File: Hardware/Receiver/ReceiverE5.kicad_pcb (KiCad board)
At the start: 2 copper layers, 50 x 30 mm, 43 parts, among them J1 KBUS, J2 AVR-PDI-6A, J3 CONN_01X08, J4 CONN_01X06, J5 CONN_01X06, J6 CONN_01X04, J7 CONN_01X04, U1 ATXMEGA32E5-A, U2 LM2731, U3 SN74LV07A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

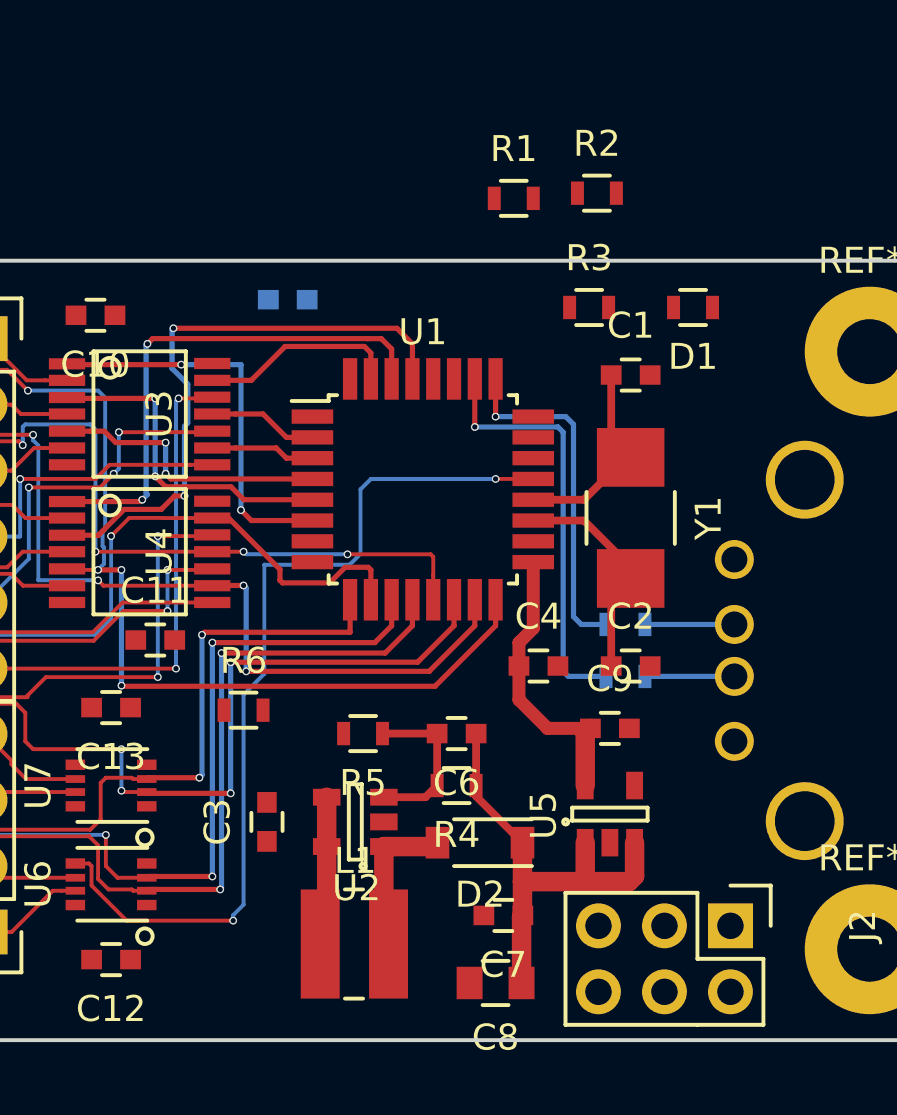
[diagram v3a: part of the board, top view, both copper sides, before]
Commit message: Finished signal routing
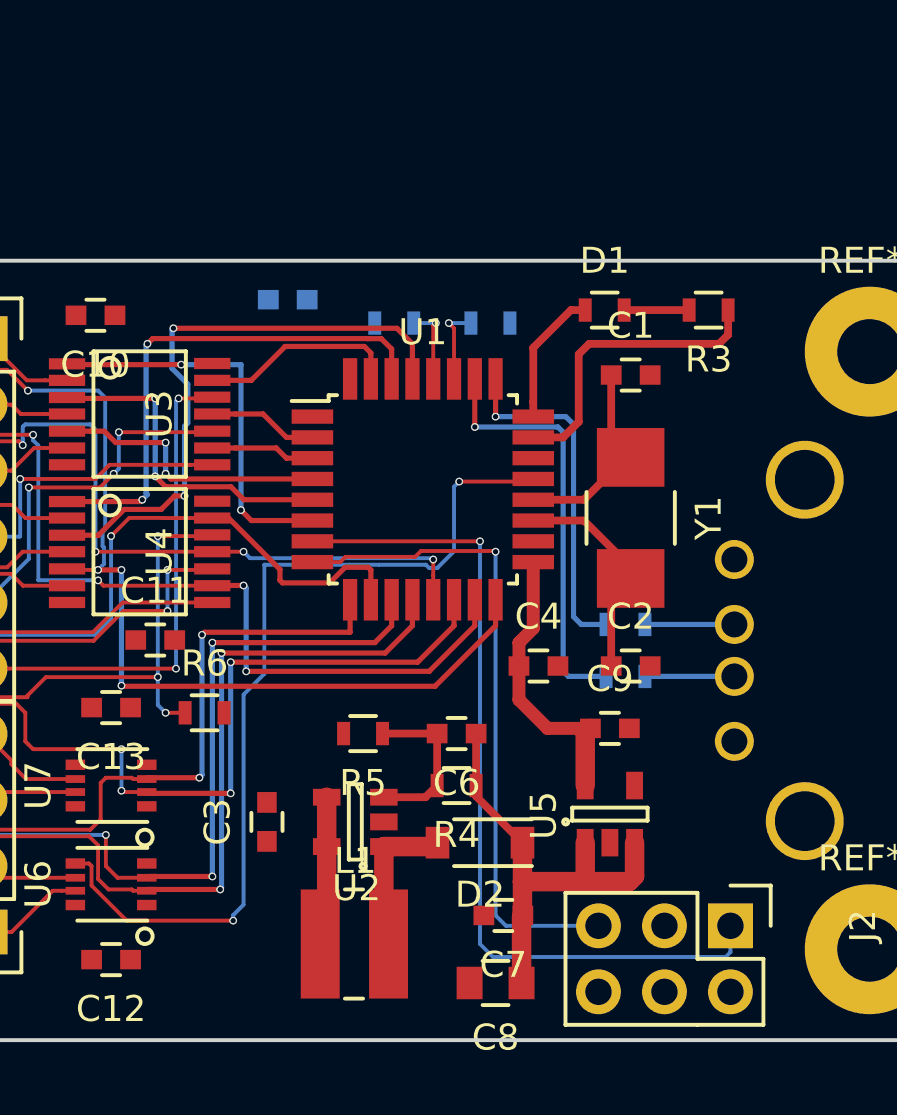
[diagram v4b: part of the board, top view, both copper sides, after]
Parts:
- R1, R2: moved to B.Cu
- moved R1 6.65 mm to (95.2, 65.4), turned to 180 degrees
- moved R2 6.47 mm to (98.9, 65.4)
- moved R3 4.60 mm to (107.3, 64.9), turned to 180 degrees
- moved D1 3.40 mm to (103.3, 64.9), turned to 0 degrees
- moved R6 1.50 mm to (87.9, 80.4)
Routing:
- net Net-(J2-Pad1): track 0.00 -> 32.9 mm, vias 0 -> 1
- net Net-(J2-Pad5): track 0.00 -> 25.4 mm, vias 0 -> 1
- net Net-(R3-Pad1): track 0.00 -> 11.6 mm
- net Net-(D1-Pad1): track 0.00 -> 5.25 mm
- net /OPT2: track 0.00 -> 3.08 mm, vias 0 -> 1
- net /OPT1: track 0.00 -> 3.04 mm, vias 0 -> 1
- net Net-(D1-Pad2): track 0.00 -> 2.50 mm
- net Net-(J5-Pad6): track 18.8 -> 21.0 mm, vias 2 -> 3

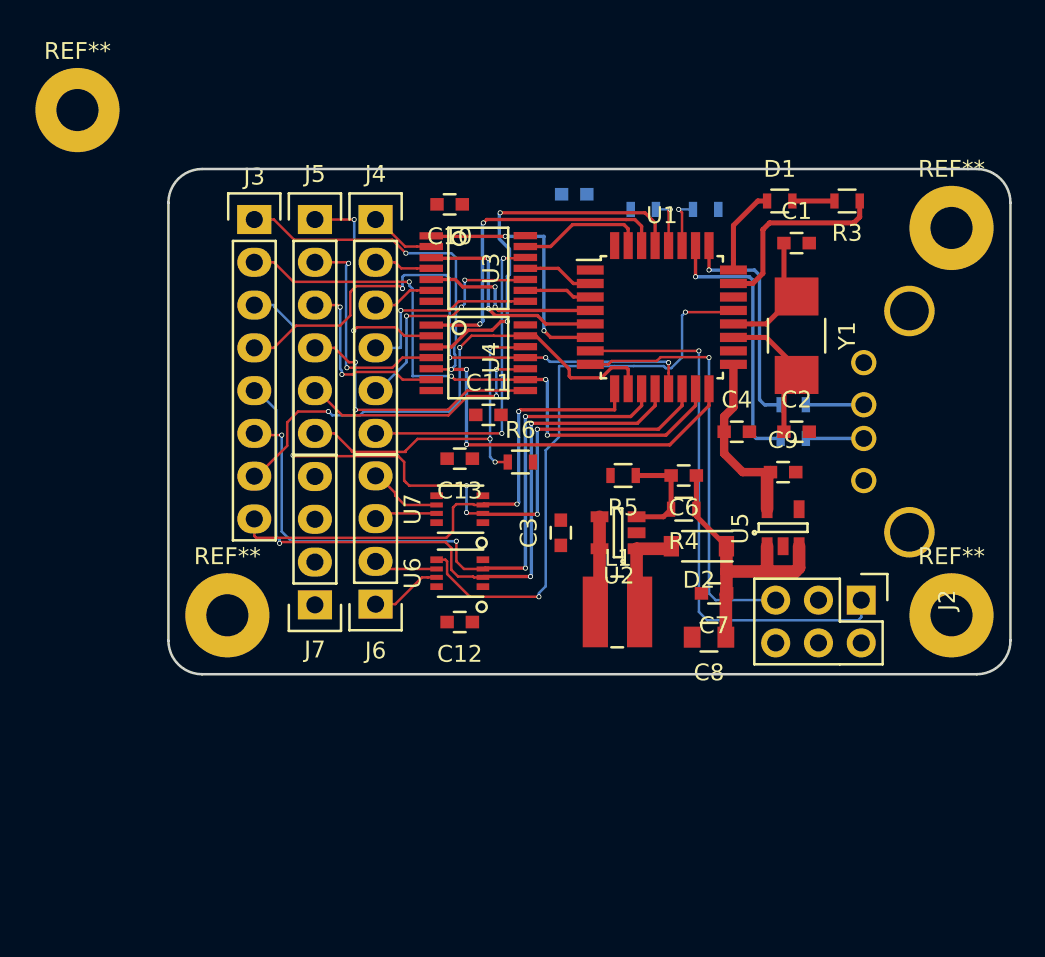
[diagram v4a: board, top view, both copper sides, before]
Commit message: 2 layer power routing part 2
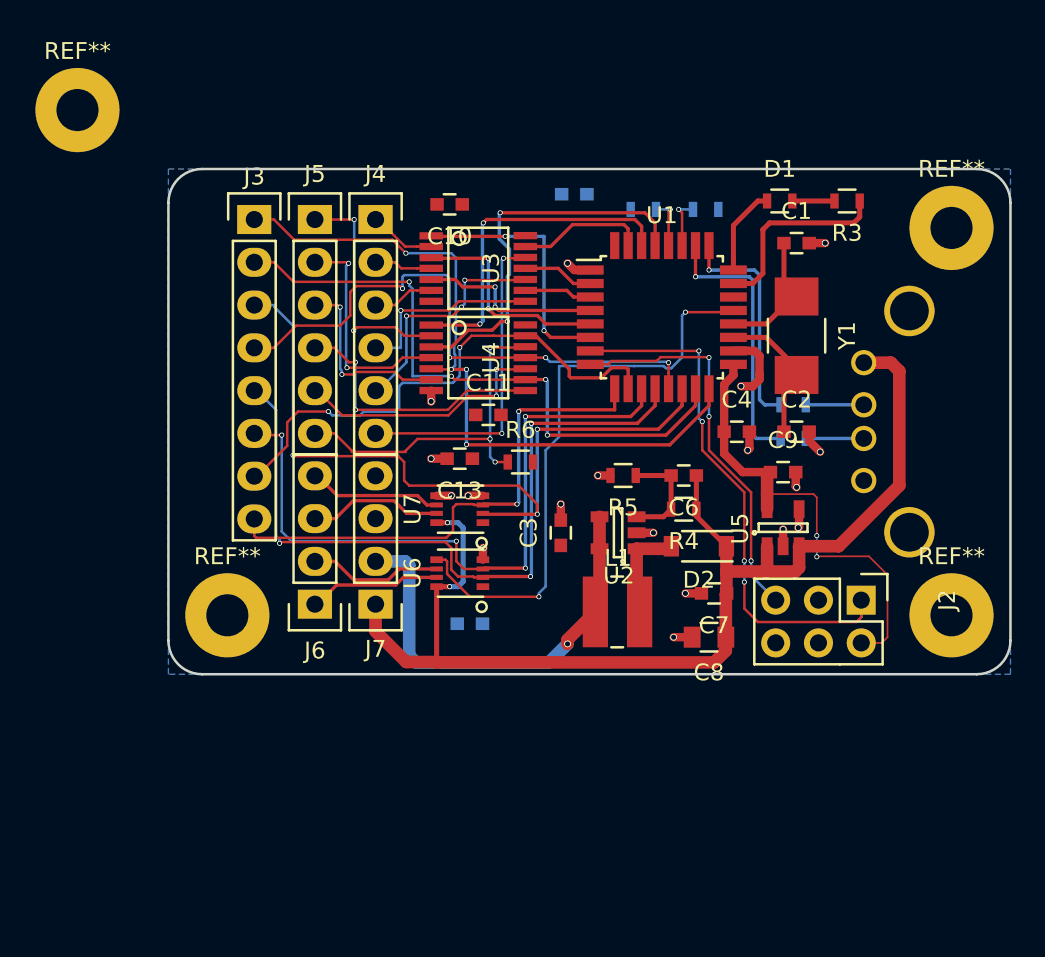
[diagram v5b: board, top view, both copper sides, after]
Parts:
- C12: moved to B.Cu
- moved J7 3.60 mm to (79.3, 88.8)
- moved J6 3.60 mm to (75.7, 88.8)
- moved C12 0.61 mm to (84.9, 90.0)
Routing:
- net +5V: track 17.6 -> 69.5 mm, vias 0 -> 2
- net GND: track 0.00 -> 21.3 mm, vias 0 -> 18
- net /BOOST_IN: track 5.75 -> 25.8 mm, vias 0 -> 1
- net +3V3: track 11.0 -> 27.6 mm, vias 0 -> 2
- net Net-(J6-Pad3): track 3.75 -> 7.98 mm
- net Net-(J6-Pad2): track 3.81 -> 7.99 mm
- net Net-(J6-Pad1): track 4.28 -> 7.88 mm
- net Net-(J6-Pad4): track 4.43 -> 7.94 mm
- net /C2: track 43.3 -> 46.0 mm, vias 5 -> 3
- net Net-(J2-Pad5): track 25.4 -> 23.3 mm, vias 1 -> 3
- net Net-(J2-Pad1): track 32.9 -> 32.5 mm, vias 1 -> 4
- added copper zone on B.Cu, net GND

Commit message: 4 layer all routed
No unrouted nets
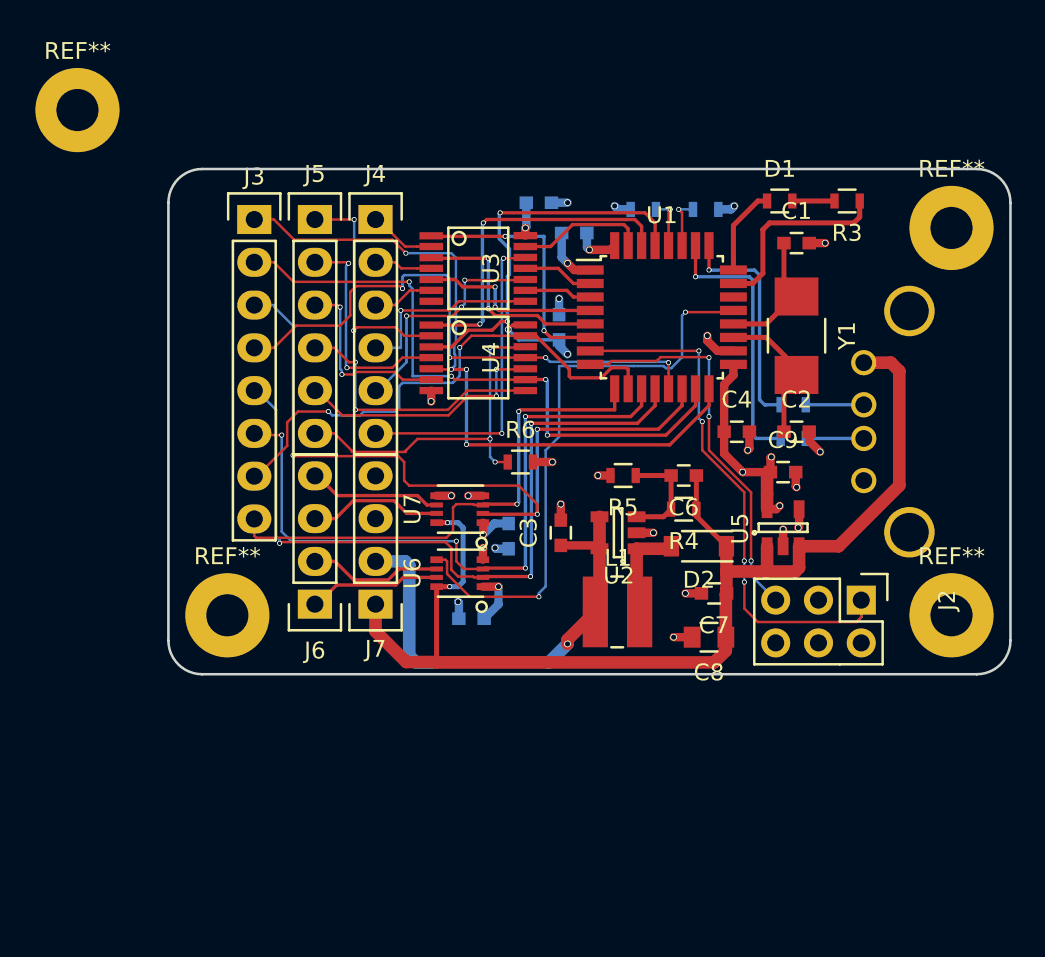
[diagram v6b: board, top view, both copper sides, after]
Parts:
- C10, C11, C13: moved to B.Cu
- moved C11 6.68 mm to (90.2, 72.4), turned to 90 degrees
- moved C13 5.44 mm to (87.2, 84.8), turned to 270 degrees
- moved C10 5.30 mm to (89.0, 65.0), turned to 0 degrees
- moved C5 2.30 mm to (91.1, 66.8)
- moved C12 0.32 mm to (85.0, 89.7)
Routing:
- net GND: track 21.3 -> 25.8 mm, vias 18 -> 23
- net /BOOST_IN: track 25.8 -> 28.2 mm
- net +3V3: track 27.6 -> 29.7 mm, vias 2 -> 10
- added copper zone on PWR.Cu, net +3V3
- added copper zone on GND.Cu, net GND
- removed copper zone on B.Cu, net GND
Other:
- copper layers 2 -> 4

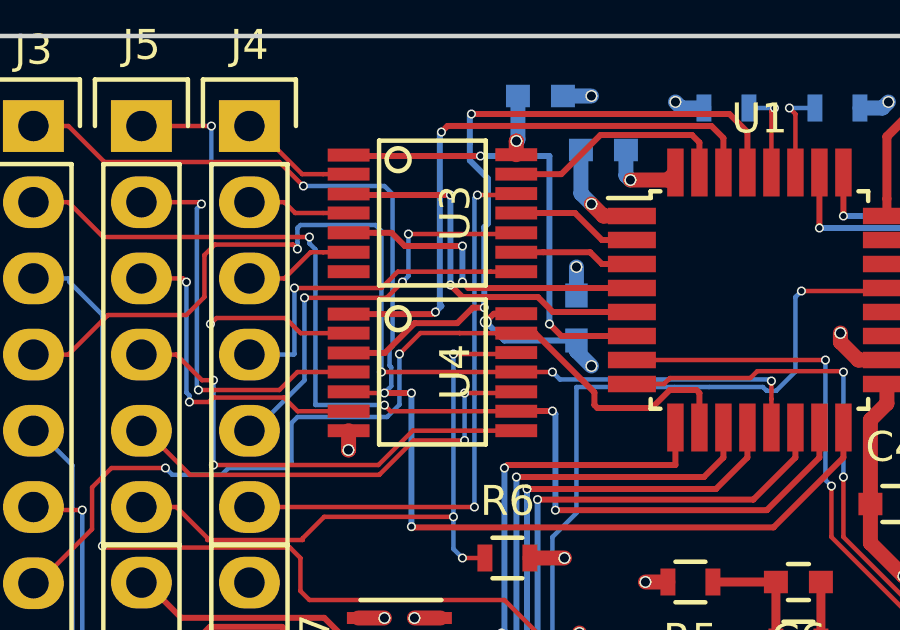
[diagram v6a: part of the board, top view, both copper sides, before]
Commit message: Unconnected net fixed, DRC passes
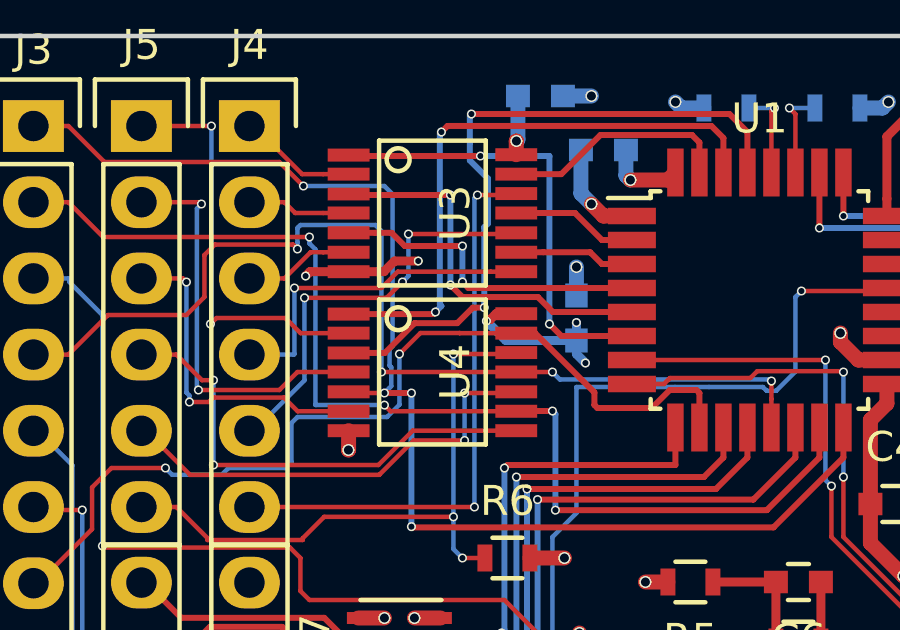
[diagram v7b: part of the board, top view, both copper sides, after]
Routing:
- net GND: track 25.8 -> 29.8 mm, vias 23 -> 25
- net +3V3: track 29.7 -> 30.1 mm, vias 10 -> 11
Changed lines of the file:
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@@
   (general
     (links 121)
-    (no_connects 60)
+    (no_connects 0)
     (area 66.924999 62.924999 117.075001 93.075001)
     (thickness 1.6)
     (drawings 11)
-    (tracks 655)
+    (tracks 666)
     (zones 0)
     (modules 43)
@@
     (32 B.Adhes user)
     (33 F.Adhes user)
-    (34 B.Paste user)
-    (35 F.Paste user)
+    (34 B.Paste user hide)
+    (35 F.Paste user hide)
     (36 B.SilkS user hide)
     (37 F.SilkS user hide)
-    (38 B.Mask user)
-    (39 F.Mask user)
+    (38 B.Mask user hide)
+    (39 F.Mask user hide)
     (40 Dwgs.User user)
     (41 Cmts.User user)
@@
   )
   (setup
-    (last_trace_width 0.5)
+    (last_trace_width 0.3)
     (user_trace_width 0.15)
     (user_trace_width 0.2)
@@
   (segment (start 102.5 72.2) (end 101.65 72.2) (width 0.3) (layer F.Cu) (net 1))
   (segment (start 101.65 72.2) (end 100.55 72.2) (width 0.3) (layer F.Cu) (net 1))
+  (segment (start 82.606 70.8558) (end 83.782304 70.8558) (width 0.3) (layer F.Cu) (net 2))
+  (segment (start 83.782304 70.8558) (end 84.138104 70.5) (width 0.3) (layer F.Cu) (net 2))
+  (segment (start 84.138104 70.5) (end 84.92741 70.5) (width 0.3) (layer F.Cu) (net 2))
+  (via (at 84.92741 70.5) (size 0.3016) (drill 0.2) (layers F.Cu B.Cu) (net 2))
+  (segment (start 82.606 70.8558) (end 81.31679 70.8558) (width 0.3) (layer F.Cu) (net 2))
+  (segment (start 81.31679 70.8558) (end 81.17259 71) (width 0.3) (layer F.Cu) (net 2))
+  (via (at 81.17259 71) (size 0.3016) (drill 0.2) (layers F.Cu B.Cu) (net 2))
   (segment (start 99.6 73.8) (end 99 73.2) (width 0.5) (layer F.Cu) (net 2))
   (segment (start 99 73.2) (end 99 72.9) (width 0.5) (layer F.Cu) (net 2))
@@
   (segment (start 92.6 89.05) (end 92.35 89.3) (width 0.75) (layer F.Cu) (net 4))
   (segment (start 92.6 83.65) (end 92.6 85.55) (width 0.75) (layer F.Cu) (net 4))
+  (segment (start 90.2 73.15) (end 90.2 72.55241) (width 0.3) (layer B.Cu) (net 5))
+  (via (at 90.2 72.55241) (size 0.3016) (drill 0.2) (layers F.Cu B.Cu) (net 5))
+  (segment (start 90.2 73.15) (end 90.2 73.6) (width 0.3) (layer B.Cu) (net 5))
+  (segment (start 90.2 73.6) (end 90.5 73.9) (width 0.3) (layer B.Cu) (net 5))
+  (via (at 90.5 73.9) (size 0.3016) (drill 0.2) (layers F.Cu B.Cu) (net 5))
+  (segment (start 87.2 72.5) (end 87.243579 72.456421) (width 0.3) (layer F.Cu) (net 5))
+  (segment (start 87.243579 72.456421) (end 87.320563 72.456421) (width 0.3) (layer F.Cu) (net 5))
+  (segment (start 87.320563 72.456421) (end 87.520084 72.2569) (width 0.3) (layer F.Cu) (net 5))
+  (segment (start 87.520084 72.2569) (end 88.194 72.2569) (width 0.3) (layer F.Cu) (net 5))
+  (segment (start 90.2 73.15) (end 87.85 73.15) (width 0.3) (layer B.Cu) (net 5))
+  (segment (start 87.85 73.15) (end 87.2 72.5) (width 0.3) (layer B.Cu) (net 5))
+  (via (at 87.2 72.5) (size 0.3016) (drill 0.2) (layers F.Cu B.Cu) (net 5))
   (segment (start 88.65 80.4) (end 89.8 80.4) (width 0.5) (layer F.Cu) (net 5))
   (via (at 89.8 80.4) (size 0.4) (drill 0.3) (layers F.Cu B.Cu) (net 5))
-  (segment (start 90.2 73.15) (end 90.2 73.5) (width 0.5) (layer B.Cu) (net 5))
-  (segment (start 90.2 73.5) (end 90.7 74) (width 0.5) (layer B.Cu) (net 5))
-  (via (at 90.7 74) (size 0.4) (drill 0.3) (layers F.Cu B.Cu) (net 5))
   (via (at 101.1 81) (size 0.4) (drill 0.3) (layers F.Cu B.Cu) (net 5))
   (segment (start 102.75 81) (end 102.75 80.15) (width 0.5) (layer F.Cu) (net 5))
@@
   (segment (start 86.35 84.05) (end 85.7 84.7) (width 0.5) (layer B.Cu) (net 5))
   (via (at 85.7 84.7) (size 0.4) (drill 0.3) (layers F.Cu B.Cu) (net 5))
-  (segment (start 90.2 73.15) (end 87.79862 73.15) (width 0.2) (layer B.Cu) (net 5))
-  (segment (start 87.79862 73.15) (end 87.17661 72.52799) (width 0.2) (layer B.Cu) (net 5))
-  (segment (start 88.194 72.2569) (end 87.4477 72.2569) (width 0.2) (layer F.Cu) (net 5))
-  (segment (start 87.4477 72.2569) (end 87.17661 72.52799) (width 0.2) (layer F.Cu) (net 5))
-  (via (at 87.17661 72.52799) (size 0.4) (drill 0.3) (layers F.Cu B.Cu) (net 5))
   (segment (start 88.25 65) (end 88.25 66.45) (width 0.5) (layer B.Cu) (net 5))
   (segment (start 88.25 66.45) (end 88.2 66.5) (width 0.5) (layer B.Cu) (net 5))
